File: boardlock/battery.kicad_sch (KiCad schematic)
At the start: 20 parts, among them J2 Conn_01x02_MountingPin, U4 BQ27441DRZR-G1A, U5 BQ24075RGT

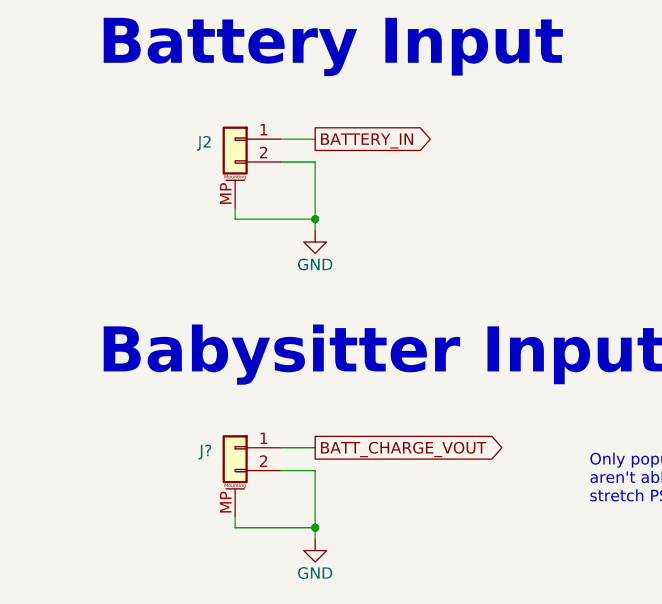
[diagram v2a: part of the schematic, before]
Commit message: footprint updates
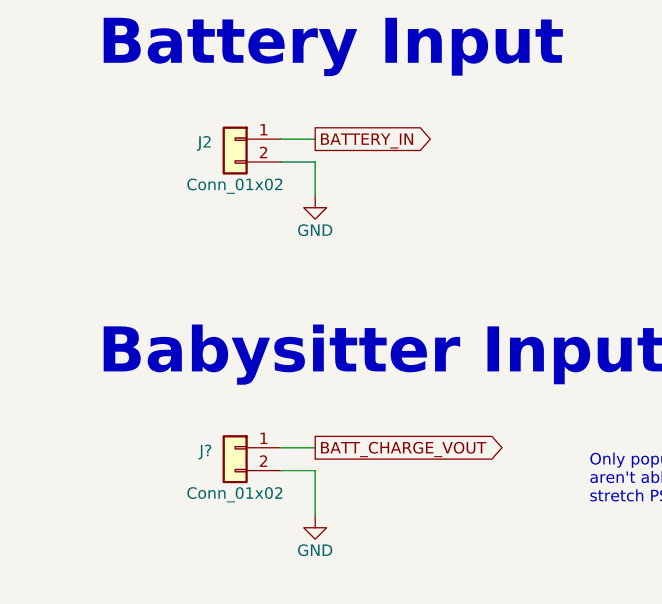
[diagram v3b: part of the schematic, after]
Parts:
- J2, J?: value Conn_01x02_MountingPin -> Conn_01x02; footprint (none) -> Connector_JST:JST_PH_S2B-PH-K_1x02_P2.00mm_Horizontal; symbol Connector_Generic_MountingPin:Conn_01x02_MountingPin -> Connector_Generic:Conn_01x02
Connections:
- net GND: no longer J2.MP (MountPin), J?.MP (MountPin)
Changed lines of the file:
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@@
   (junction (at 196.85 125.73) (diameter 0) (color 0 0 0 0)
   )
-  (junction (at 60.96 177.8) (diameter 0) (color 0 0 0 0)
-  )
   (junction (at 58.42 66.04) (diameter 0) (color 0 0 0 0)
   )
@@
   (junction (at 121.92 97.79) (diameter 0) (color 0 0 0 0)
   )
-  (junction (at 60.96 143.51) (diameter 0) (color 0 0 0 0)
-  )
   (junction (at 83.82 45.72) (diameter 0) (color 0 0 0 0)
   )
@@
     (stroke (width 0) (type default))
   )
-  (wire (pts (xy 52.07 177.8) (xy 60.96 177.8))
-    (stroke (width 0) (type default))
-  )
   (wire (pts (xy 179.07 135.89) (xy 184.15 135.89))
     (stroke (width 0) (type default))
@@
     (stroke (width 0) (type default))
   )
-  (wire (pts (xy 60.96 171.45) (xy 60.96 177.8))
-    (stroke (width 0) (type default))
-  )
-  (wire (pts (xy 60.96 177.8) (xy 60.96 179.07))
+  (wire (pts (xy 60.96 171.45) (xy 60.96 176.53))
     (stroke (width 0) (type default))
   )
@@
     (stroke (width 0) (type default))
   )
-  (wire (pts (xy 52.07 142.24) (xy 52.07 143.51))
-    (stroke (width 0) (type default))
-  )
   (wire (pts (xy 83.82 46.99) (xy 83.82 45.72))
     (stroke (width 0) (type default))
@@
     (stroke (width 0) (type default))
   )
-  (wire (pts (xy 52.07 176.53) (xy 52.07 177.8))
-    (stroke (width 0) (type default))
-  )
   (wire (pts (xy 184.15 130.81) (xy 184.15 135.89))
     (stroke (width 0) (type default))
@@
     (stroke (width 0) (type default))
   )
-  (wire (pts (xy 52.07 143.51) (xy 60.96 143.51))
-    (stroke (width 0) (type default))
-  )
   (wire (pts (xy 198.12 143.51) (xy 200.66 143.51))
     (stroke (width 0) (type default))
@@
     (stroke (width 0) (type default))
   )
-  (wire (pts (xy 60.96 137.16) (xy 60.96 143.51))
+  (wire (pts (xy 60.96 137.16) (xy 60.96 140.97))
     (stroke (width 0) (type default))
   )
@@
   )
   (wire (pts (xy 213.36 152.4) (xy 213.36 153.67))
-    (stroke (width 0) (type default))
-  )
-  (wire (pts (xy 60.96 143.51) (xy 60.96 144.78))
     (stroke (width 0) (type default))
   )
@@
     )
   )
-  (symbol (lib_id "Connector_Generic_MountingPin:Conn_01x02_MountingPin") (at 52.07 134.62 0) (mirror y) (unit 1)
+  (symbol (lib_id "Connector_Generic:Conn_01x02") (at 52.07 134.62 0) (mirror y) (unit 1)
     (in_bom yes) (on_board yes) (dnp no)
     (property "Reference" "J2" (at 49.53 134.9756 0)
       (effects (font (size 1.27 1.27)) (justify left))
     )
-    (property "Value" "Conn_01x02_MountingPin" (at 49.53 137.5156 90)
-      (effects (font (size 1.27 1.27)) (justify right) hide)
-    )
-    (property "Footprint" "" (at 52.07 134.62 0)
+    (property "Value" "Conn_01x02" (at 52.07 139.7 0)
+      (effects (font (size 1.27 1.27)))
+    )
+    (property "Footprint" "Connector_JST:JST_PH_S2B-PH-K_1x02_P2.00mm_Horizontal" (at 52.07 134.62 0)
       (effects (font (size 1.27 1.27)) hide)
     )
@@
     (pin "1")
     (pin "2")
-    (pin "MP")
     (instances
       (project "boardlock"
@@
     )
   )
-  (symbol (lib_id "power:GND") (at 60.96 144.78 0) (mirror y) (unit 1)
-    (in_bom yes) (on_board yes) (dnp no)
-    (property "Reference" "#PWR035" (at 60.96 151.13 0)
-      (effects (font (size 1.27 1.27)) hide)
-    )
-    (property "Value" "GND" (at 60.96 148.59 0)
-      (effects (font (size 1.27 1.27)))
-    )
-    (property "Footprint" "" (at 60.96 144.78 0)
-      (effects (font (size 1.27 1.27)) hide)
-    )
-    (property "Datasheet" "" (at 60.96 144.78 0)
+  (symbol (lib_id "power:GND") (at 60.96 140.97 0) (mirror y) (unit 1)
+    (in_bom yes) (on_board yes) (dnp no)
+    (property "Reference" "#PWR035" (at 60.96 147.32 0)
+      (effects (font (size 1.27 1.27)) hide)
+    )
+    (property "Value" "GND" (at 60.96 144.78 0)
+      (effects (font (size 1.27 1.27)))
+    )
+    (property "Footprint" "" (at 60.96 140.97 0)
+      (effects (font (size 1.27 1.27)) hide)
+    )
+    (property "Datasheet" "" (at 60.96 140.97 0)
       (effects (font (size 1.27 1.27)) hide)
     )
@@
     )
   )
-  (symbol (lib_id "Connector_Generic_MountingPin:Conn_01x02_MountingPin") (at 52.07 168.91 0) (mirror y) (unit 1)
+  (symbol (lib_id "Connector_Generic:Conn_01x02") (at 52.07 168.91 0) (mirror y) (unit 1)
     (in_bom yes) (on_board yes) (dnp no)
     (property "Reference" "J?" (at 49.53 169.2656 0)
       (effects (font (size 1.27 1.27)) (justify left))
     )
-    (property "Value" "Conn_01x02_MountingPin" (at 49.53 171.8056 90)
-      (effects (font (size 1.27 1.27)) (justify right) hide)
-    )
-    (property "Footprint" "" (at 52.07 168.91 0)
+    (property "Value" "Conn_01x02" (at 52.07 173.99 0)
+      (effects (font (size 1.27 1.27)))
+    )
+    (property "Footprint" "Connector_JST:JST_PH_S2B-PH-K_1x02_P2.00mm_Horizontal" (at 52.07 168.91 0)
       (effects (font (size 1.27 1.27)) hide)
     )
@@
     (pin "1")
     (pin "2")
-    (pin "MP")
     (instances
       (project "boardlock"
@@
     )
   )
-  (symbol (lib_id "power:GND") (at 60.96 179.07 0) (mirror y) (unit 1)
-    (in_bom yes) (on_board yes) (dnp no)
-    (property "Reference" "#PWR024" (at 60.96 185.42 0)
-      (effects (font (size 1.27 1.27)) hide)
-    )
-    (property "Value" "GND" (at 60.96 182.88 0)
-      (effects (font (size 1.27 1.27)))
-    )
-    (property "Footprint" "" (at 60.96 179.07 0)
-      (effects (font (size 1.27 1.27)) hide)
-    )
-    (property "Datasheet" "" (at 60.96 179.07 0)
-      (effects (font (size 1.27 1.27)) hide)
-    )
+  (symbol (lib_id "power:GND") (at 60.96 176.53 0) (mirror y) (unit 1)
+    (in_bom yes) (on_board yes) (dnp no)
+    (property "Reference" "#PWR024" (at 60.96 182.88 0)
+      (effects (font (size 1.27 1.27)) hide)
+    )
+    (property "Value" "GND" (at 60.96 180.34 0)
+      (effects (font (size 1.27 1.27)))
+    )
+    (property "Footprint" "" (at 60.96 176.53 0)
+      (effects (font (size 1.27 1.27)) hide)
+    )
+    (property "Datasheet" "" (at 60.96 176.53 0)
+      (effects (font (size 1.27 1.27)) hide)
+    )

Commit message: footprint work
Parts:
- gave numbers to parts that had none: 14
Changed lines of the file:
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@@
   (symbol (lib_id "Device:R_US") (at 76.2 92.71 0) (unit 1)
     (in_bom yes) (on_board yes) (dnp no) (fields_autoplaced)
-    (property "Reference" "R?" (at 78.74 91.44 0)
+    (property "Reference" "R48" (at 78.74 91.44 0)
       (effects (font (size 1.27 1.27)) (justify left))
     )
@@
       (project "boardlock"
         (path "/e1fc29ce-837e-4062-84d8-c7e423f9eab9/a05f4dcd-7a18-4529-a05e-43353e81fbf8"
-          (reference "R?") (unit 1)
+          (reference "R48") (unit 1)
         )
       )
@@
   (symbol (lib_id "Device:R_US") (at 236.22 120.65 0) (unit 1)
     (in_bom yes) (on_board yes) (dnp no) (fields_autoplaced)
-    (property "Reference" "R?" (at 238.76 119.38 0)
+    (property "Reference" "R49" (at 238.76 119.38 0)
       (effects (font (size 1.27 1.27)) (justify left))
     )
@@
       (project "boardlock"
         (path "/e1fc29ce-837e-4062-84d8-c7e423f9eab9/a05f4dcd-7a18-4529-a05e-43353e81fbf8"
-          (reference "R?") (unit 1)
+          (reference "R49") (unit 1)
         )
         (path "/e1fc29ce-837e-4062-84d8-c7e423f9eab9"
@@
   (symbol (lib_id "Device:C") (at 257.81 138.43 0) (unit 1)
     (in_bom yes) (on_board yes) (dnp no) (fields_autoplaced)
-    (property "Reference" "C?" (at 261.62 137.16 0)
+    (property "Reference" "C21" (at 261.62 137.16 0)
       (effects (font (size 1.27 1.27)) (justify left))
     )
@@
       (project "boardlock"
         (path "/e1fc29ce-837e-4062-84d8-c7e423f9eab9/a05f4dcd-7a18-4529-a05e-43353e81fbf8"
-          (reference "C?") (unit 1)
+          (reference "C21") (unit 1)
         )
       )
@@
   (symbol (lib_id "Device:R_US") (at 137.16 33.02 0) (unit 1)
     (in_bom yes) (on_board yes) (dnp no) (fields_autoplaced)
-    (property "Reference" "R?" (at 139.7 31.75 0)
+    (property "Reference" "R40" (at 139.7 31.75 0)
       (effects (font (size 1.27 1.27)) (justify left))
     )
@@
       (project "boardlock"
         (path "/e1fc29ce-837e-4062-84d8-c7e423f9eab9/a05f4dcd-7a18-4529-a05e-43353e81fbf8"
-          (reference "R?") (unit 1)
+          (reference "R40") (unit 1)
         )
       )
@@
   (symbol (lib_id "Device:R_US") (at 189.23 125.73 270) (unit 1)
     (in_bom yes) (on_board yes) (dnp no) (fields_autoplaced)
-    (property "Reference" "R?" (at 189.23 119.38 90)
+    (property "Reference" "R50" (at 189.23 119.38 90)
       (effects (font (size 1.27 1.27)))
     )
@@
       (project "boardlock"
         (path "/e1fc29ce-837e-4062-84d8-c7e423f9eab9/a05f4dcd-7a18-4529-a05e-43353e81fbf8"
-          (reference "R?") (unit 1)
+          (reference "R50") (unit 1)
         )
       )
@@
   (symbol (lib_id "Device:R_US") (at 137.16 46.99 0) (unit 1)
     (in_bom yes) (on_board yes) (dnp no) (fields_autoplaced)
-    (property "Reference" "R?" (at 139.7 45.72 0)
+    (property "Reference" "R43" (at 139.7 45.72 0)
       (effects (font (size 1.27 1.27)) (justify left))
     )
@@
       (project "boardlock"
         (path "/e1fc29ce-837e-4062-84d8-c7e423f9eab9/a05f4dcd-7a18-4529-a05e-43353e81fbf8"
-          (reference "R?") (unit 1)
+          (reference "R43") (unit 1)
         )
       )
@@
   (symbol (lib_id "Device:R_US") (at 210.82 64.77 0) (unit 1)
     (in_bom yes) (on_board yes) (dnp no) (fields_autoplaced)
-    (property "Reference" "R?" (at 213.36 63.5 0)
+    (property "Reference" "R44" (at 213.36 63.5 0)
       (effects (font (size 1.27 1.27)) (justify left))
     )
@@
       (project "boardlock"
         (path "/e1fc29ce-837e-4062-84d8-c7e423f9eab9/a05f4dcd-7a18-4529-a05e-43353e81fbf8"
-          (reference "R?") (unit 1)
+          (reference "R44") (unit 1)
         )
       )
@@
   (symbol (lib_id "Device:R_US") (at 199.39 35.56 0) (unit 1)
     (in_bom yes) (on_board yes) (dnp no) (fields_autoplaced)
-    (property "Reference" "R?" (at 201.93 34.29 0)
+    (property "Reference" "R42" (at 201.93 34.29 0)
       (effects (font (size 1.27 1.27)) (justify left))
     )
@@
       (project "boardlock"
         (path "/e1fc29ce-837e-4062-84d8-c7e423f9eab9/a05f4dcd-7a18-4529-a05e-43353e81fbf8"
-          (reference "R?") (unit 1)
+          (reference "R42") (unit 1)
         )
       )
@@
   (symbol (lib_id "Device:C") (at 179.07 140.97 0) (unit 1)
     (in_bom yes) (on_board yes) (dnp no)
-    (property "Reference" "C?" (at 172.72 139.7 0)
+    (property "Reference" "C25" (at 172.72 139.7 0)
       (effects (font (size 1.27 1.27)) (justify left))
     )
@@
       (project "boardlock"
         (path "/e1fc29ce-837e-4062-84d8-c7e423f9eab9/a05f4dcd-7a18-4529-a05e-43353e81fbf8"
-          (reference "C?") (unit 1)
+          (reference "C25") (unit 1)
         )
       )
@@
   (symbol (lib_id "Device:R_US") (at 110.49 91.44 0) (unit 1)
     (in_bom yes) (on_board yes) (dnp no)
-    (property "Reference" "R?" (at 113.03 90.17 0)
+    (property "Reference" "R45" (at 113.03 90.17 0)
       (effects (font (size 1.27 1.27)) (justify left))
     )
@@
       (project "boardlock"
         (path "/e1fc29ce-837e-4062-84d8-c7e423f9eab9/a05f4dcd-7a18-4529-a05e-43353e81fbf8"
-          (reference "R?") (unit 1)
+          (reference "R45") (unit 1)
         )
       )
@@
   (symbol (lib_id "Connector_Generic:Conn_01x02") (at 52.07 168.91 0) (mirror y) (unit 1)
     (in_bom yes) (on_board yes) (dnp no)
-    (property "Reference" "J?" (at 49.53 169.2656 0)
+    (property "Reference" "J1" (at 49.53 169.2656 0)
       (effects (font (size 1.27 1.27)) (justify left))
     )
@@
       (project "boardlock"
         (path "/e1fc29ce-837e-4062-84d8-c7e423f9eab9/a05f4dcd-7a18-4529-a05e-43353e81fbf8"
-          (reference "J?") (unit 1)
+          (reference "J1") (unit 1)
         )
       )
@@
   (symbol (lib_id "Device:R_US") (at 121.92 91.44 0) (unit 1)
     (in_bom yes) (on_board yes) (dnp no)
-    (property "Reference" "R?" (at 124.46 90.17 0)
+    (property "Reference" "R46" (at 124.46 90.17 0)
       (effects (font (size 1.27 1.27)) (justify left))
     )
@@
       (project "boardlock"
         (path "/e1fc29ce-837e-4062-84d8-c7e423f9eab9/a05f4dcd-7a18-4529-a05e-43353e81fbf8"
-          (reference "R?") (unit 1)
+          (reference "R46") (unit 1)
         )
       )
@@
   (symbol (lib_id "Device:R_US") (at 189.23 35.56 0) (unit 1)
     (in_bom yes) (on_board yes) (dnp no) (fields_autoplaced)
-    (property "Reference" "R?" (at 191.77 34.29 0)
+    (property "Reference" "R41" (at 191.77 34.29 0)
       (effects (font (size 1.27 1.27)) (justify left))
     )
@@
       (project "boardlock"
         (path "/e1fc29ce-837e-4062-84d8-c7e423f9eab9/a05f4dcd-7a18-4529-a05e-43353e81fbf8"
-          (reference "R?") (unit 1)
+          (reference "R41") (unit 1)
         )
       )
@@
   (symbol (lib_id "Device:R_US") (at 66.04 92.71 0) (unit 1)
     (in_bom yes) (on_board yes) (dnp no) (fields_autoplaced)
-    (property "Reference" "R?" (at 68.58 91.44 0)
+    (property "Reference" "R47" (at 68.58 91.44 0)
       (effects (font (size 1.27 1.27)) (justify left))
     )
@@
       (project "boardlock"
         (path "/e1fc29ce-837e-4062-84d8-c7e423f9eab9/a05f4dcd-7a18-4529-a05e-43353e81fbf8"
-          (reference "R?") (unit 1)
-        )
-      )
+          (reference "R47") (unit 1)
+        )
+      )

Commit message: footprints finished for now
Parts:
- C18, C19, C20, C21, C25: footprint (none) -> Capacitor_SMD:C_0805_2012Metric_Pad1.18x1.45mm_HandSolder
- R40, R43: footprint (none) -> Resistor_SMD:R_0805_2012Metric_Pad1.20x1.40mm_HandSolder
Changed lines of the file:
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@@
       (effects (font (size 1.27 1.27)) (justify left))
     )
-    (property "Footprint" "" (at 84.7852 54.61 0)
+    (property "Footprint" "Capacitor_SMD:C_0805_2012Metric_Pad1.18x1.45mm_HandSolder" (at 84.7852 54.61 0)
       (effects (font (size 1.27 1.27)) hide)
     )
@@
       (effects (font (size 1.27 1.27)) (justify left))
     )
-    (property "Footprint" "" (at 258.7752 142.24 0)
+    (property "Footprint" "Capacitor_SMD:C_0805_2012Metric_Pad1.18x1.45mm_HandSolder" (at 258.7752 142.24 0)
       (effects (font (size 1.27 1.27)) hide)
     )
@@
       (effects (font (size 1.27 1.27)) (justify left))
     )
-    (property "Footprint" "" (at 59.3852 74.93 0)
+    (property "Footprint" "Capacitor_SMD:C_0805_2012Metric_Pad1.18x1.45mm_HandSolder" (at 59.3852 74.93 0)
       (effects (font (size 1.27 1.27)) hide)
     )
@@
       (effects (font (size 1.27 1.27)) (justify left))
     )
-    (property "Footprint" "" (at 138.176 33.274 90)
+    (property "Footprint" "Resistor_SMD:R_0805_2012Metric_Pad1.20x1.40mm_HandSolder" (at 138.176 33.274 90)
       (effects (font (size 1.27 1.27)) hide)
     )
@@
       (effects (font (size 1.27 1.27)) (justify left))
     )
-    (property "Footprint" "" (at 144.4752 74.93 0)
+    (property "Footprint" "Capacitor_SMD:C_0805_2012Metric_Pad1.18x1.45mm_HandSolder" (at 144.4752 74.93 0)
       (effects (font (size 1.27 1.27)) hide)
     )
@@
       (effects (font (size 1.27 1.27)) (justify left))
     )
-    (property "Footprint" "" (at 138.176 47.244 90)
+    (property "Footprint" "Resistor_SMD:R_0805_2012Metric_Pad1.20x1.40mm_HandSolder" (at 138.176 47.244 90)
       (effects (font (size 1.27 1.27)) hide)
     )
@@
       (effects (font (size 1.27 1.27)) (justify left))
     )
-    (property "Footprint" "" (at 180.0352 144.78 0)
-      (effects (font (size 1.27 1.27)) hide)
-    )
+    (property "Footprint" "Capacitor_SMD:C_0805_2012Metric_Pad1.18x1.45mm_HandSolder" (at 180.0352 144.78 0)
+      (effects (font (size 1.27 1.27)) hide)
+    )
